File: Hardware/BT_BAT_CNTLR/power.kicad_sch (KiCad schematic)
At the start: 10 parts, among them J1 Barrel_Jack_Switch

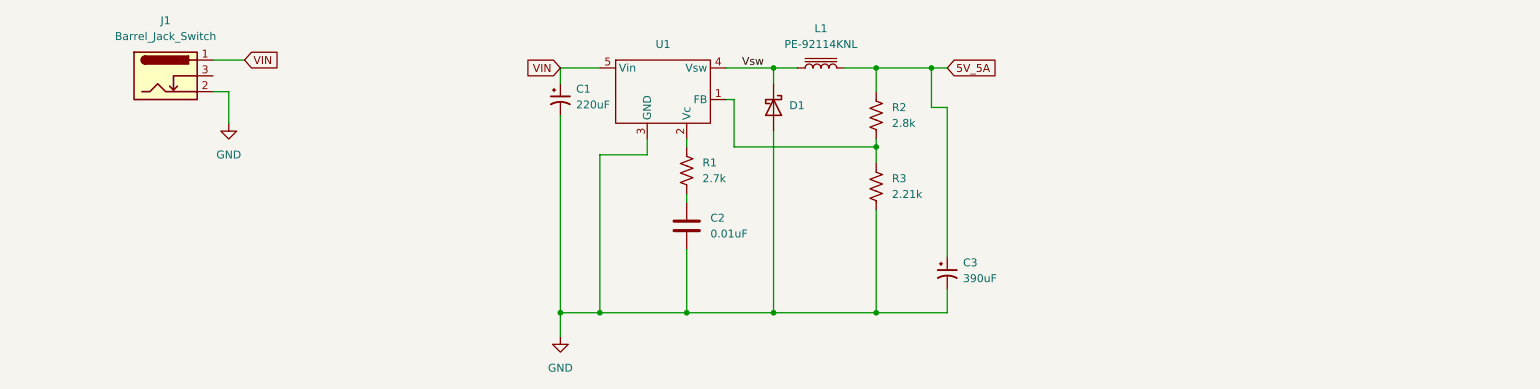
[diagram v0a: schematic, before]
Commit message: dead ass think I just added a second copy..
aight. routed caps and antenna for nRF.
need to route power and find a new IC for USB ports.
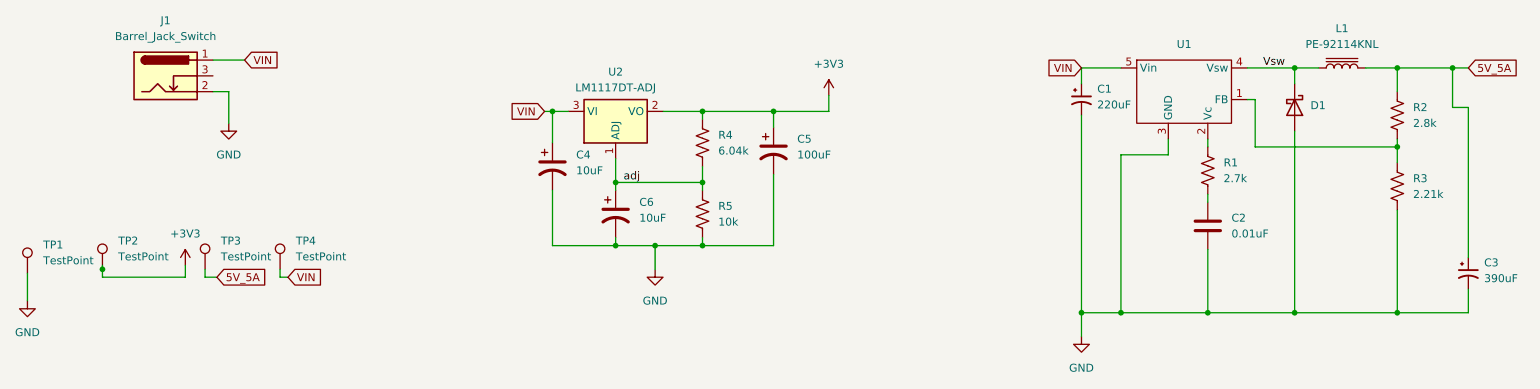
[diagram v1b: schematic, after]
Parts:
- added C4, C6: 10uF, Capacitor_SMD:CP_Elec_4x4.5, symbol Device:C_Polarized_US
- added C5: 100uF, Capacitor_SMD:CP_Elec_6.3x5.2, symbol Device:C_Polarized_US
- added R4: 6.04k, Resistor_SMD:R_0603_1608Metric, symbol Device:R_US
- added R5: 10k, Resistor_SMD:R_0603_1608Metric, symbol Device:R_US
- added TP1, TP2, TP3, TP4: TestPoint, TestPoint:TestPoint_Pad_D1.0mm, symbol Connector:TestPoint
- added U2: LM1117DT-ADJ, Package_TO_SOT_SMD:TO-252-3_TabPin2, symbol Regulator_Linear:LM1117DT-ADJ
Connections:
- net 5V_5A: now also TP3.1
- net GND: now also C4.2, C5.2, C6.2, R5.2, TP1.1
- net VIN: now also C4.1, TP4.1, U2.3 (VI)
- new net +3V3: C5.1, R4.1, TP2.1, U2.2 (VO)
- new net adj: C6.1, R4.2, R5.1, U2.1 (ADJ)
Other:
- moved on the sheet: C1, C2, C3, D1, L1, R1, R2, R3, U1

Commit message: - Github Tree Cleanup - Power Routing
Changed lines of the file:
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@@
   (junction (at 214.63 80.01) (diameter 0) (color 0 0 0 0)
   )
-  (junction (at 36.83 73.025) (diameter 0) (color 0 0 0 0)
-  )
   (junction (at 133.35 69.215) (diameter 0) (color 0 0 0 0)
   )
@@
     (stroke (width 0) (type default))
   )
-  (wire (pts (xy 36.83 74.295) (xy 36.83 73.025))
+  (wire (pts (xy 36.83 73.025) (xy 36.83 74.93))
     (stroke (width 0) (type default))
   )
@@
     (stroke (width 0) (type default))
   )
-  (wire (pts (xy 50.165 72.39) (xy 50.165 74.295))
+  (wire (pts (xy 50.165 72.39) (xy 50.165 74.93))
     (stroke (width 0) (type default))
   )
@@
     (stroke (width 0) (type default))
   )
-  (wire (pts (xy 50.165 74.295) (xy 36.83 74.295))
-    (stroke (width 0) (type default))
-  )
-  (wire (pts (xy 36.83 73.025) (xy 36.83 72.39))
+  (wire (pts (xy 50.165 74.93) (xy 36.83 74.93))
     (stroke (width 0) (type default))
   )
@@
       (effects (font (size 1.27 1.27)) hide)
     )
+    (pin "1")
+    (pin "2")
     (pin "3")
-    (pin "1")
-    (pin "2")
     (instances
       (project "BT_BAT_CNTLR"
@@
       (effects (font (size 1.27 1.27)) hide)
     )
+    (pin "1")
+    (pin "2")
+    (pin "3")
     (pin "4")
-    (pin "1")
-    (pin "2")
-    (pin "3")
     (pin "5")
     (instances
@@
       (effects (font (size 1.27 1.27)) hide)
     )
-    (pin "2")
-    (pin "1")
+    (pin "1")
+    (pin "2")
     (instances
       (project "BT_BAT_CNTLR"
@@
       (effects (font (size 1.27 1.27)) hide)
     )
-    (pin "2")
-    (pin "1")
+    (pin "1")
+    (pin "2")
     (instances
       (project "BT_BAT_CNTLR"
@@
       (effects (font (size 1.27 1.27)) hide)
     )
-    (pin "2")
-    (pin "1")
+    (pin "1")
+    (pin "2")
     (instances
       (project "BT_BAT_CNTLR"
@@
       (effects (font (size 1.27 1.27)) hide)
     )
-    (pin "2")
-    (pin "1")
+    (pin "1")
+    (pin "2")
     (instances
       (project "BT_BAT_CNTLR"
@@
       (effects (font (size 1.27 1.27)) hide)
     )
+    (pin "1")
     (pin "2")
     (pin "3")
-    (pin "1")
     (instances
       (project "BT_BAT_CNTLR"
@@
       (effects (font (size 1.27 1.27)) hide)
     )
-    (pin "2")
-    (pin "1")
+    (pin "1")
+    (pin "2")
     (instances
       (project "BT_BAT_CNTLR"
@@
       (effects (font (size 1.27 1.27)) hide)
     )
-    (pin "2")
-    (pin "1")
+    (pin "1")
+    (pin "2")
     (instances
       (project "BT_BAT_CNTLR"
@@
       (effects (font (size 1.27 1.27)) hide)
     )
-    (pin "2")
-    (pin "1")
+    (pin "1")
+    (pin "2")
     (instances
       (project "BT_BAT_CNTLR"
@@
       (effects (font (size 1.27 1.27)) hide)
     )
-    (pin "2")
-    (pin "1")
-    (instances
-      (project "BT_BAT_CNTLR"
+    (pin "1")
+    (pin "2")
+    (instances
+      (project "BT_BAT_CNTLR"
